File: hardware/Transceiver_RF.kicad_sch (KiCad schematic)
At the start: 42 parts, among them J12 Conn_Coaxial, J14 Conn_01x01, J5 Conn_Coaxial, J6 Conn_Coaxial, J7 Conn_Coaxial, J8 Conn_Coaxial, J9 Conn_Coaxial, U3 AD9361, X3 SiT1602B

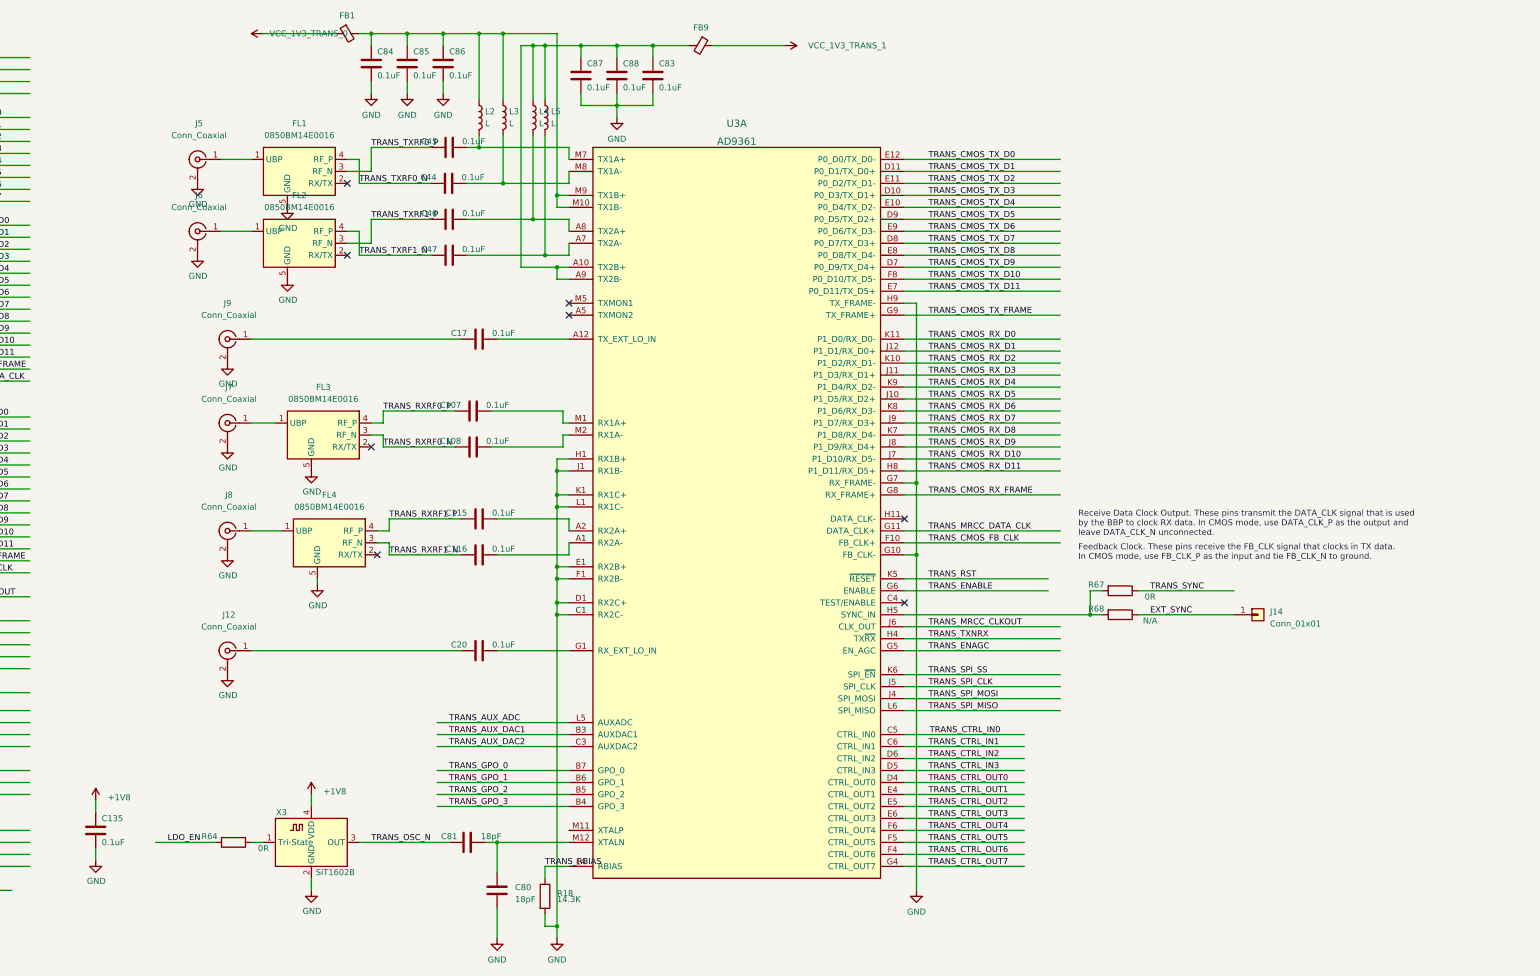
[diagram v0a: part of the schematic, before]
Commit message: delete RF transceiver
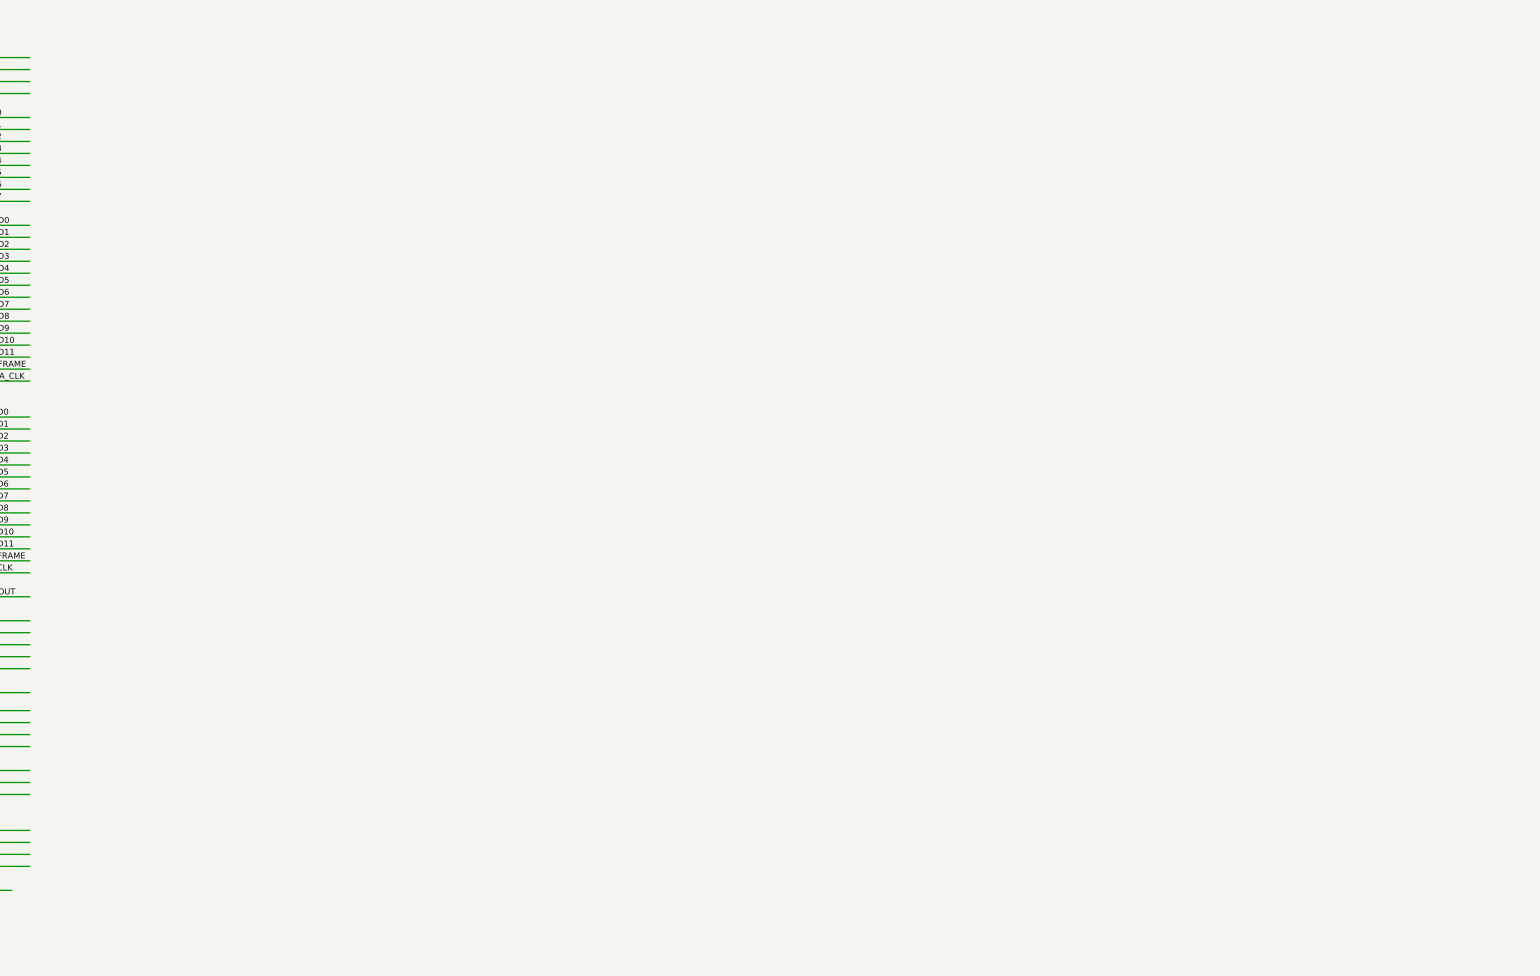
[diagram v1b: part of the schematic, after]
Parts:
- removed C107, C108, C115, C116, C135, C17, C20, C44, C45, C46, C47, C83, C84, C85, C86, C87, C88: 0.1uF, Capacitor_SMD:C_0201_0603Metric, symbol Device:C
- removed C80, C81: 18pF, Capacitor_SMD:C_0201_0603Metric, symbol Device:C
- removed FB1, FB9: FerriteBead_Small, Capacitor_SMD:C_0402_1005Metric, symbol Device:FerriteBead_Small
- removed FL1, FL2, FL3, FL4: 0850BM14E0016, RF_Converter:Balun_Johanson_1.6x0.8mm, symbol Filter:0850BM14E0016
- removed J12, J5, J6, J7, J8, J9: Conn_Coaxial, Connector_Coaxial_Local:U.FL_Molex_MCRF_73412-0110_Vertical, symbol Connector:Conn_Coaxial
- removed J14: Conn_01x01, Connector_PinHeader_2.54mm:PinHeader_1x01_P2.54mm_Vertical, symbol Connector_Generic:Conn_01x01
- removed L2, L3, L4, L5: L, Inductor_SMD:L_0402_1005Metric, symbol Device:L
- removed R18: 14.3K, Resistor_SMD:R_0201_0603Metric, symbol Device:R
- removed R64, R67: 0R, Resistor_SMD:R_0201_0603Metric, symbol Device:R
- removed R68: N/A, Resistor_SMD:R_0201_0603Metric, symbol Device:R
- removed U3: AD9361, RF_Transceiver:bga-100_10_10_1p32_0p8, symbol 7z010_ddr:AD9361
- removed X3: SiT1602B, Oscillator:Oscillator_SMD_ECS_2520MV-xxx-xx-4Pin_2.5x2.0mm, symbol 7z010_ddr:ECS-2520MV-xxx-xx
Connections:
- no-connect marks 8 -> 0
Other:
- note removed: "Feedback Clock. These pins receive the FB_CLK signal that clocks in TX data. In CMOS mode, use FB_CLK_P as the input and tie FB_CLK_N to ground."
- note removed: "Receive Data Clock Output. These pins transmit the DATA_CLK signal that is used by the BBP to clock RX data. In CMOS mode, use DATA_CLK_P as the output and leave DATA_CLK_N unconnected."
